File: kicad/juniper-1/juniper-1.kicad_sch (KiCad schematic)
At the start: 36 parts

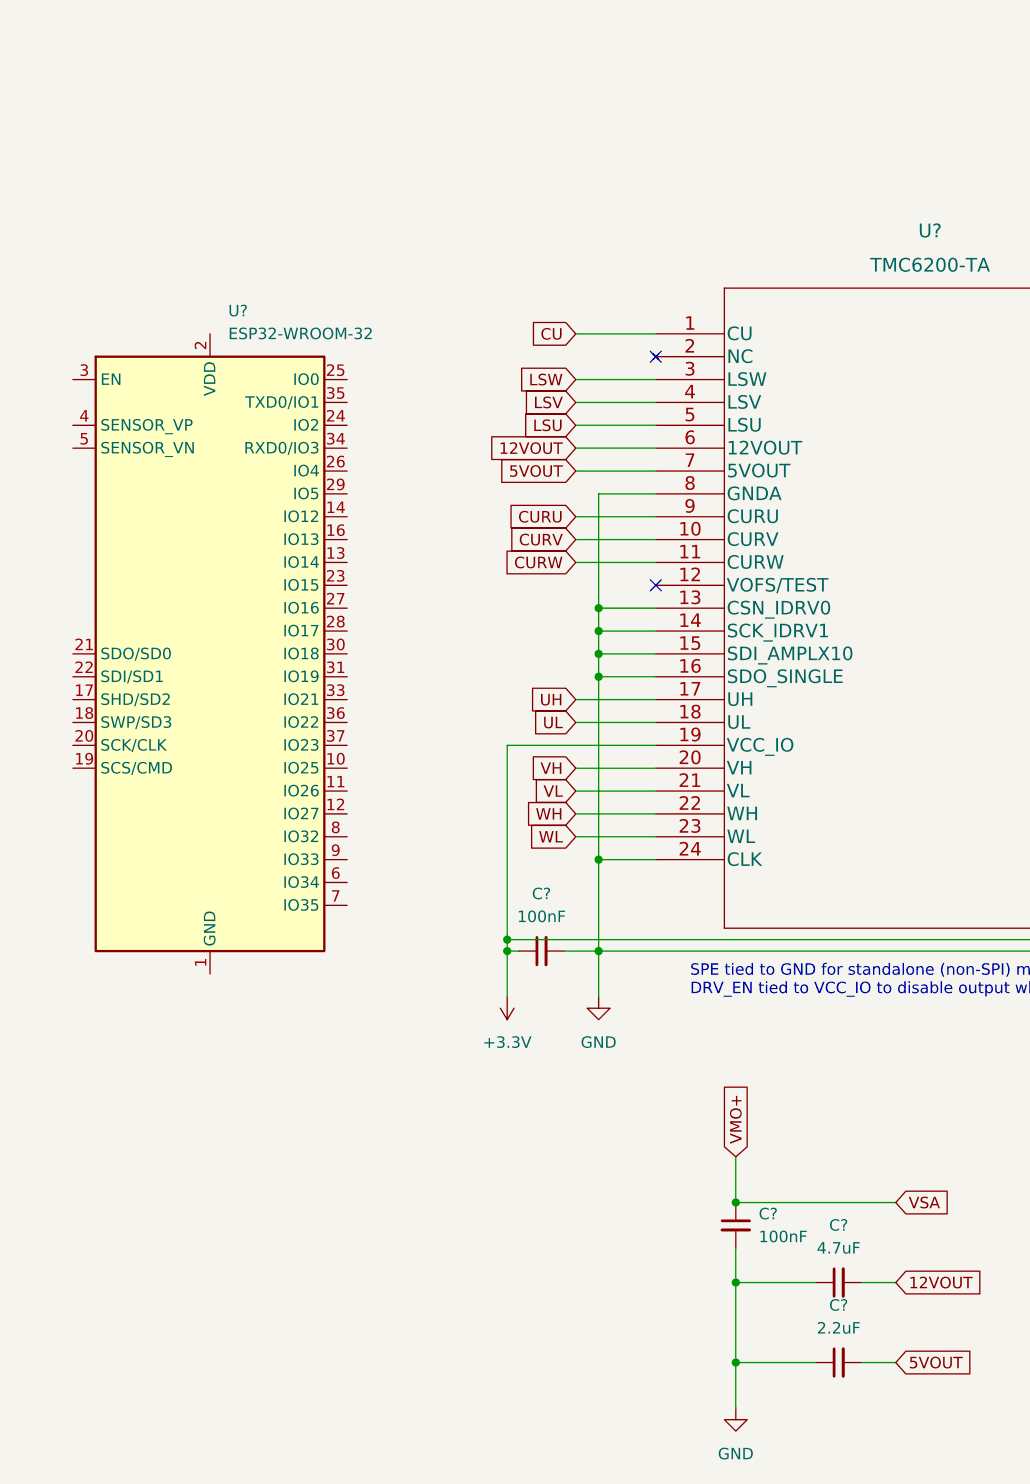
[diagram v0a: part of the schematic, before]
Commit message: added power supply for ESP32, haven't yet finished assigning esp32 pins
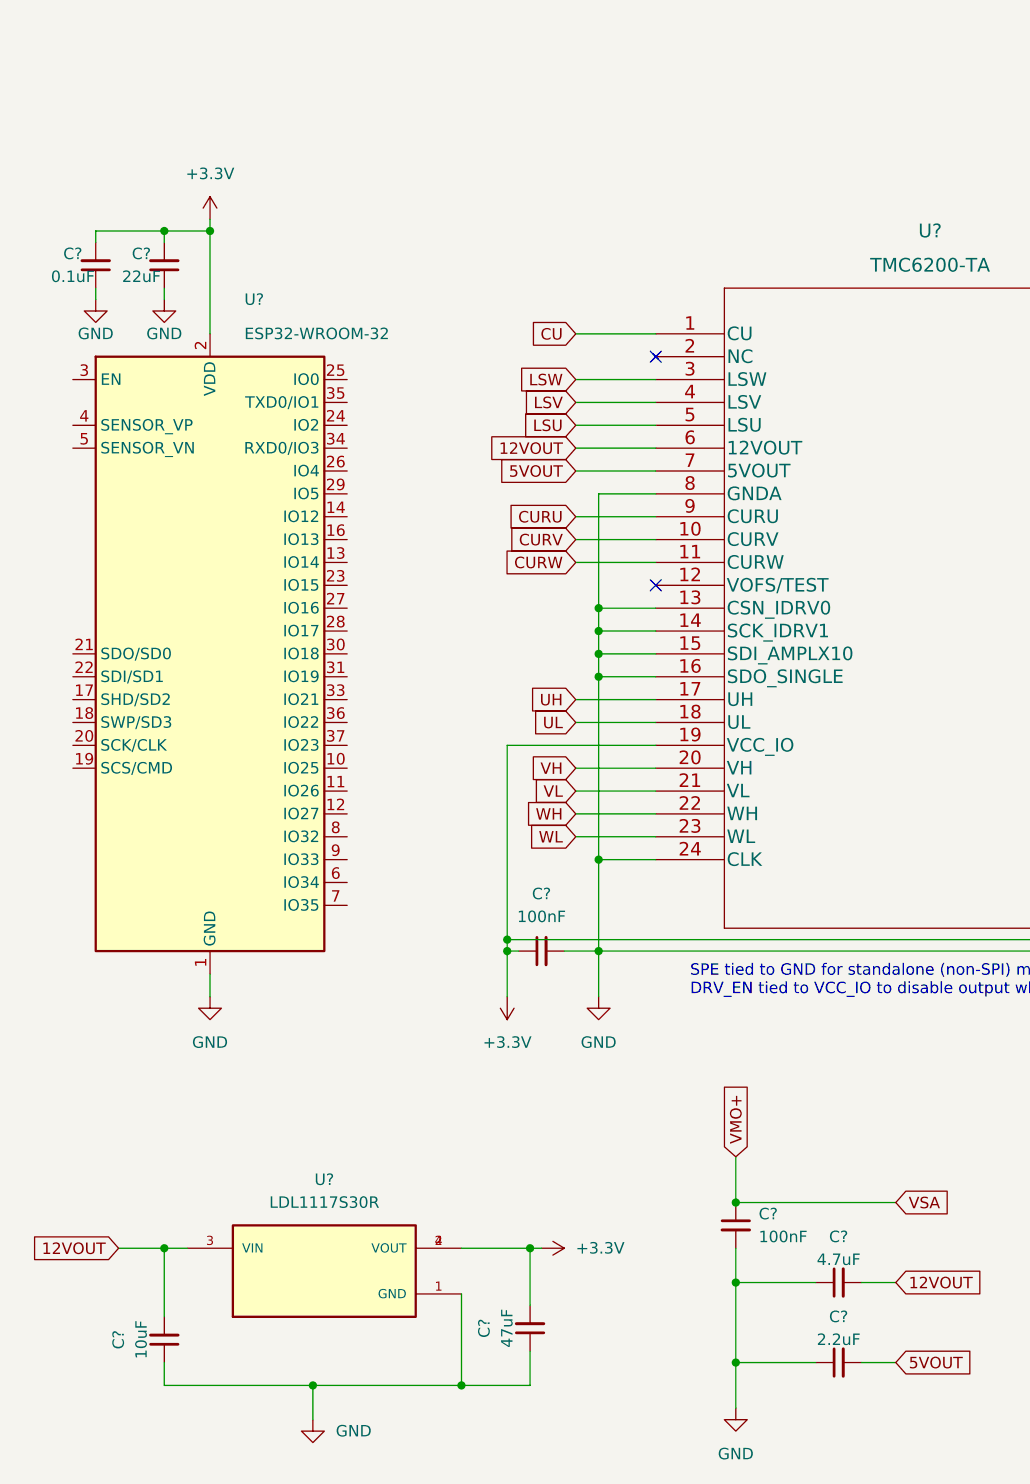
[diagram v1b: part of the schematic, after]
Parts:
- added C?: 0.1uF, symbol Device:C_Small
- added C?: 22uF, symbol Device:C_Small
- added C?: 47uF, symbol Device:C_Small
- added C?: 10uF, symbol Device:C_Small
- added U?: LDL1117S30R, SOT230P700X180-4N, symbol LDL1117S30R:LDL1117S30R
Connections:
- net +3.3V: now also U?.2 (VDD), C?.2, C?.2, C?.2, U?.2 (VOUT), U?.4 (VOUT)
- net 12VOUT: now also C?.2, U?.3 (VIN)
- net GND: now also U?.1 (GND), U?.15 (GND), U?.38 (GND), U?.39 (GND), C?.1, C?.1, C?.1, C?.1, U?.1 (GND)

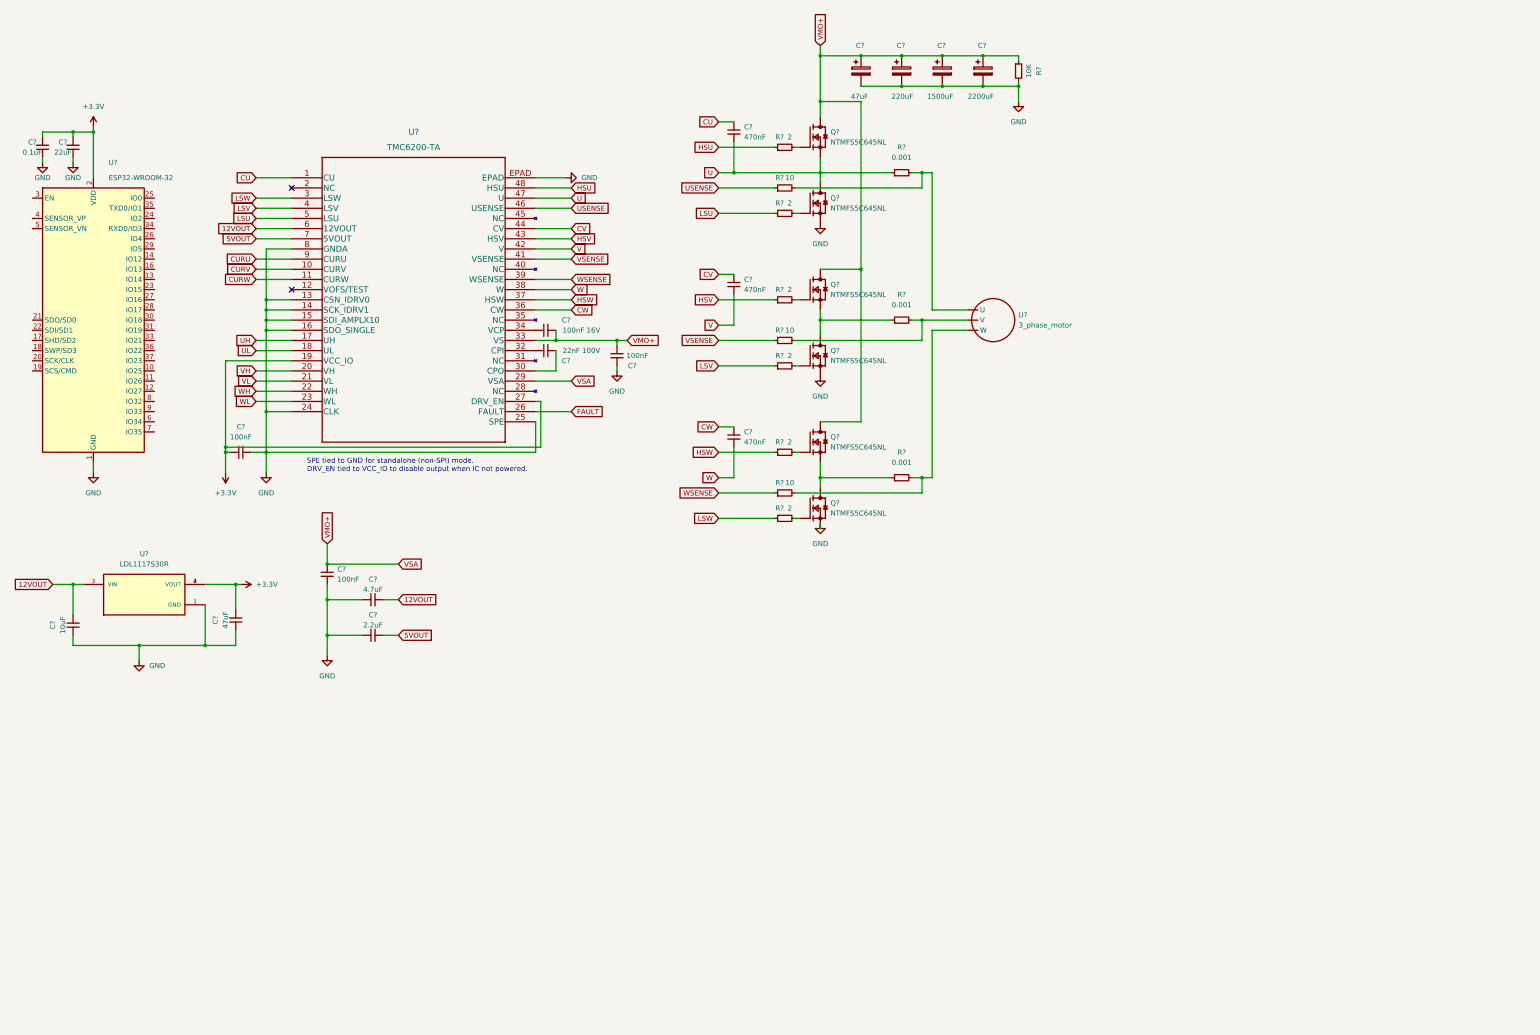
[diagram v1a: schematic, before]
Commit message: fixed esp32 symbol, nearly finished assigning pins for MCU
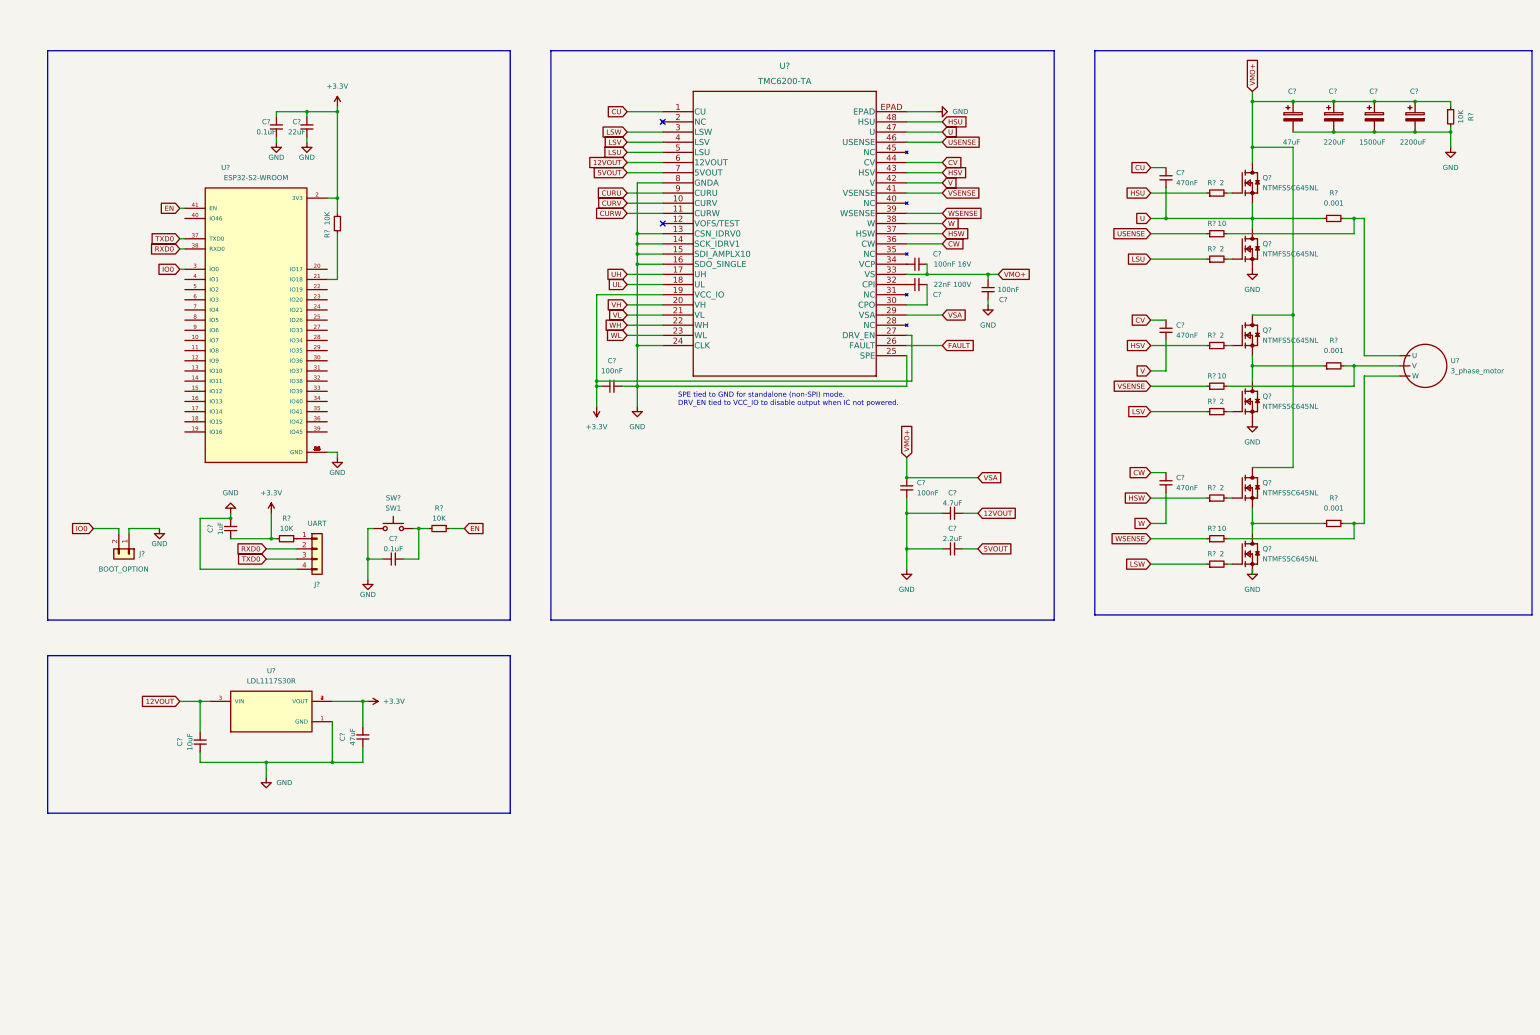
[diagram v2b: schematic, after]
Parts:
- removed U?: ESP32-WROOM-32, RF_Module:ESP32-WROOM-32, symbol RF_Module:ESP32-WROOM-32
- added C?: 1uF, symbol Device:C_Small
- added C?: 0.1uF, symbol Device:C_Small
- added J?: UART, symbol Connector_Generic:Conn_01x04
- added J?: BOOT_OPTION, symbol Connector_Generic:Conn_01x02
- added R? (x3): 10K, symbol Device:R_Small
- added SW?: SW1, symbol Switch:SW_Push
- added U?: ESP32-S2-WROOM, XCVR_ESP32-S2-WROOM, symbol ESP32-S2-WROOM:ESP32-S2-WROOM
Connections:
- net +3.3V: now also C?.1, R?.2, R?.2, U?.2 (3V3)
- net GND: now also C?.1, C?.2, J?.1 (Pin_1), J?.4 (Pin_4), SW?.1, U?.1 (GND), U?.26 (GND), U?.42 (GND), U?.43 (GND), U?.44 (GND), U?.45 (GND), U?.46 (GND), U?.47 (GND), U?.48 (GND), U?.49 (GND), U?.50 (GND), U?.51 (GND)
- new net: J?.1 (Pin_1), R?.1
- new net: C?.2, R?.2, SW?.2
- new net: R?.1, U?.21 (IO18)
- new net EN: R?.1, U?.41 (EN)
- new net IO0: J?.2 (Pin_2), U?.3 (IO0)
- new net RXD0: J?.2 (Pin_2), U?.38 (RXD0)
- new net TXD0: J?.3 (Pin_3), U?.37 (TXD0)
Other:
- moved on the sheet: C?, Q?, R?, U?

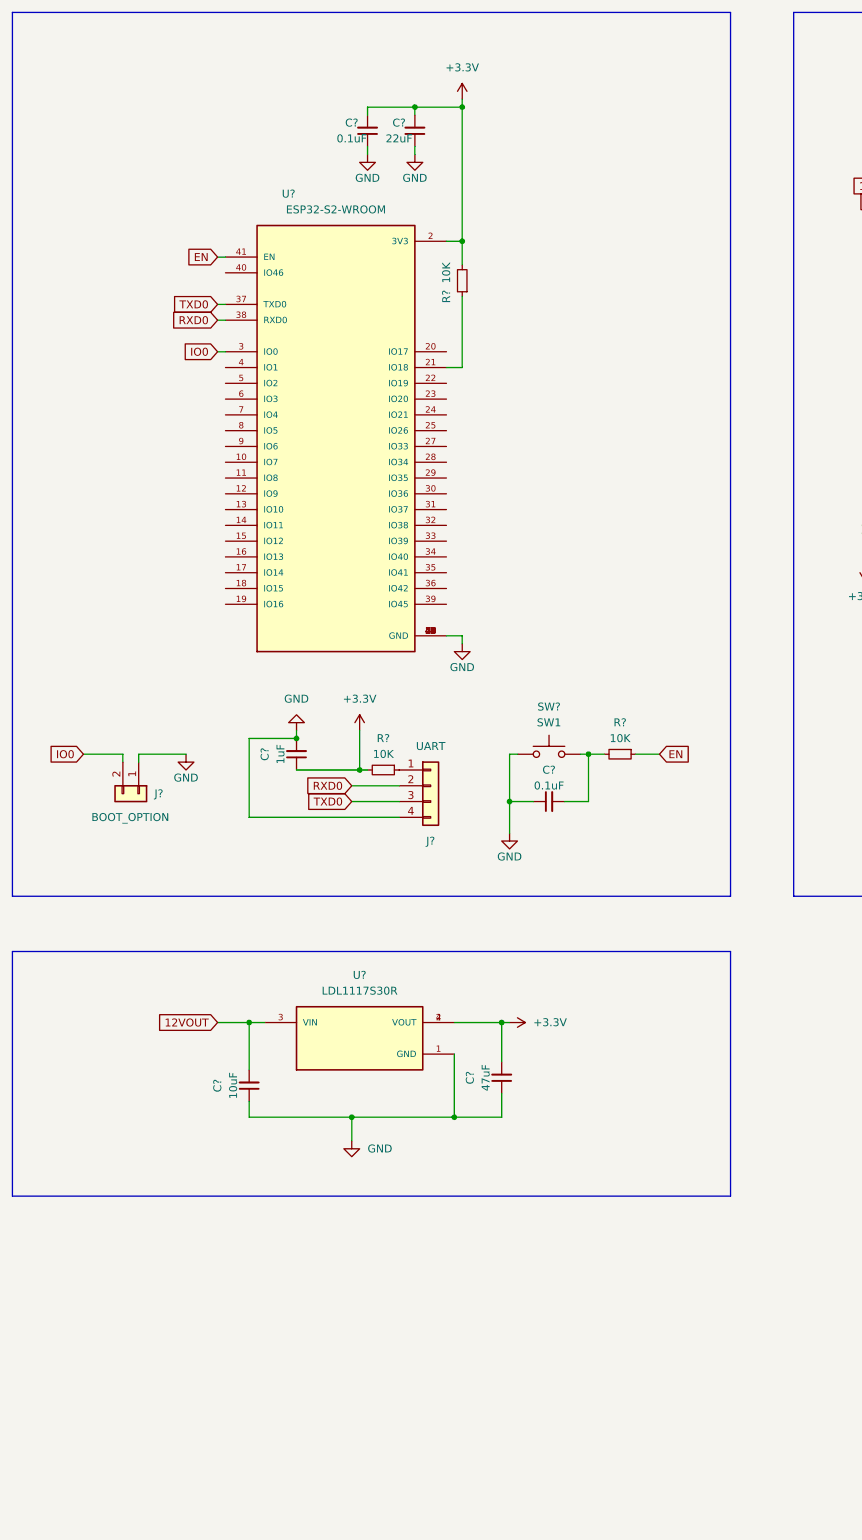
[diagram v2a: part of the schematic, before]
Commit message: Fixed voltage regulator, organized, added text, added encoder input
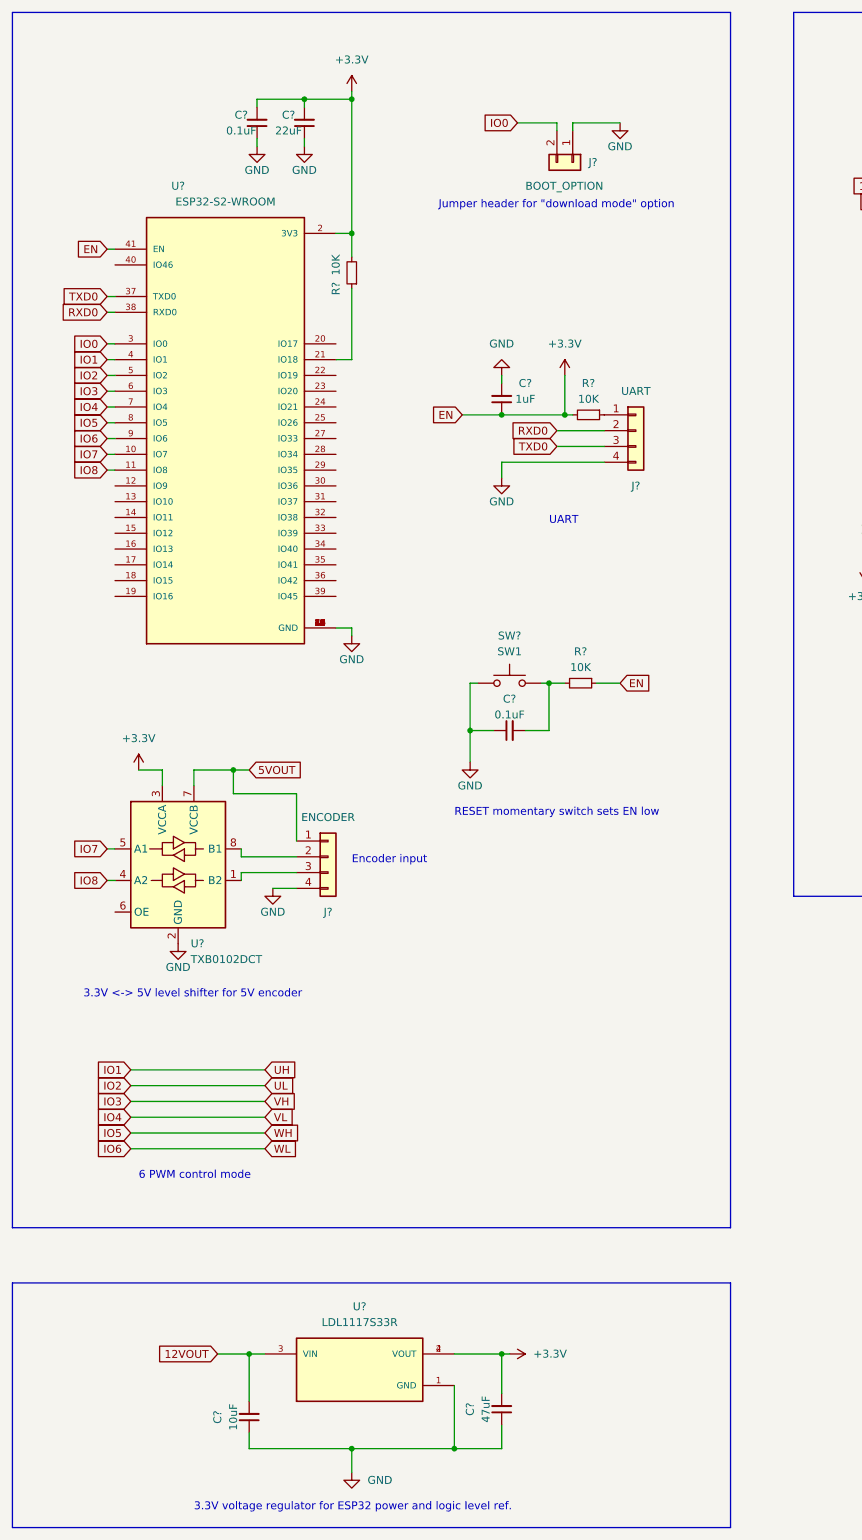
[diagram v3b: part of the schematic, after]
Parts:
- added J?: ENCODER, symbol Connector_Generic:Conn_01x04
- added U?: TXB0102DCT, Package_SO:TSSOP-8_3x3mm_P0.65mm, symbol Logic_LevelTranslator:TXB0102DCT
- U?: value LDL1117S30R -> LDL1117S33R
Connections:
- net EN is gone; now on net +3.3V: R?.1, U?.41 (EN)
- net UH is gone; now on net IO1: U?.17 (UH)
- net UL is gone; now on net IO2: U?.18 (UL)
- net VH is gone; now on net IO3: U?.20 (VH)
- net VL is gone; now on net IO4: U?.21 (VL)
- net WH is gone; now on net IO5: U?.22 (WH)
- net WL is gone; now on net IO6: U?.23 (WL)
- net +3.3V: now also U?.3 (VCCA)
- net 5VOUT: now also J?.1 (Pin_1), U?.7 (VCCB)
- net GND: now also J?.4 (Pin_4), U?.2 (GND)
- net IO7: now reaches U?.10 (IO7)
- net IO7: now also U?.5 (A1)
- net IO8: now reaches U?.11 (IO8)
- net IO8: now also U?.4 (A2)
- net IO1: now reaches U?.4 (IO1)
- net IO2: now reaches U?.5 (IO2)
- net IO3: now reaches U?.6 (IO3)
- net IO4: now reaches U?.7 (IO4)
- net IO5: now reaches U?.8 (IO5)
- net IO6: now reaches U?.9 (IO6)
- new net: J?.3 (Pin_3), U?.1 (B2)
- new net: J?.2 (Pin_2), U?.8 (B1)
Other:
- note added: "3.3V <-> 5V level shifter for 5V encoder"
- note added: "3.3V voltage regulator for ESP32 power and logic level ref."
- note added: "6 PWM control mode"
- note added: "Encoder input"
- note added: "Jumper header for "download mode" option"
- note added: "RESET momentary switch sets EN low"
- note added: "UART"
- moved on the sheet: C?, J?, R?, SW?, U?
